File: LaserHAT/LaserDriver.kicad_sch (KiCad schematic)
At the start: 25 parts, among them J1 GPIO, J6 Conn_Coaxial, J7 Conn_Coaxial, U1 CAT24C32, U4 MCP1700x-330xxMB

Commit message: LaserHAT Rev 2: hand-routed HAT, laser + e-stim daughterboards, fab outputs
HAT (LaserHAT/):
- Rev 1 -> Rev 2 schematic migration (tools/rev2_migrate.py): issue #3 fixes,
  OLED bonnet kept, analog stage moved to plug-in daughterboards (J8/J9),
  buffered BNC I/O, USB-C power switch + PFET ideal diode.
- MCU pin map re-optimised for fewest vias: Pi UART on UART1 (PA8/PA9), I2C on
  PA0/PA1 (fail-safe), PWM_A/B on TIMA0 CCP1/CCP3 (PA7/PA12) with FAULT0 on PA6,
  active-low buttons.  Pi header: SWD swapped, NRST <-> MCU_POWER_EN swapped.
- Stable symbol UUIDs so KiCad "Update PCB" never replaces footprints.
- PCB placed and routed by hand; tidied (tools/track_tidy.py), silkscreen
  decluttered (tools/silk_declutter.py).  DRC clean apart from known cosmetic items.
- JLC fab outputs regenerated (fab/LaserHAT).
- CLAUDE.md, REV2_NOTES.md updated; portable Claude memory in claude_memory/.

Daughterboards: LaserDaughter (300 mA laser driver) and EStimDaughter (isolated
e-stim, imported from kbest/estim_module); interface spec in estim_interface/.

Firmware/Pi: `make flash HAT_REV=2` selects the Rev 2 header wiring;
Pi/power_cycle.py takes its power/reset pins from the environment.

Co-Authored-By: Claude Opus 5.5 <noreply@anthropic.com>
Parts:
- removed D10: D_Zener 6.2V, Diode_SMD:D_SOD-523, symbol Device:D_Zener
- removed D11: LED_ABGR, LED_SMD:LED_RGB_1210, symbol Device:LED_ABGR
- removed D6: 3v3, Diode_SMD:D_0603_1608Metric, symbol Device:LED
- removed D9: STIM, Diode_SMD:D_0603_1608Metric, symbol Device:LED
- removed J6, J7: Conn_Coaxial, Connector_Coaxial:BNC_Amphenol_031-5539_Vertical, symbol Connector:Conn_Coaxial
- removed R14: 200, Resistor_SMD:R_0402_1005Metric, symbol Device:R
- removed R16, R18: 470, Resistor_SMD:R_0402_1005Metric, symbol Device:R
- removed R17: 1k 1%, Resistor_SMD:R_0402_1005Metric, symbol Device:R
- added JP5: STANDALONE_3V3, Jumper:SolderJumper-2_P1.3mm_Open_RoundedPad1.0x1.5mm, symbol Jumper:SolderJumper_2_Open
- added R19, R20: 4.7k, Resistor_SMD:R_0402_1005Metric, symbol Device:R
- D7: value MSPM0 -> MCU
- JP4: value ID_WP -> RTS_NRST
- R13: value 1k 1% -> 3k
- R15: value 200 -> 2k
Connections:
- net +3V3: now also JP5.1 (A)
- net MCU_UART_RX: no longer J1.10 (Pin_10)
- net MCU_UART_TX: no longer J1.8 (Pin_8)
- net RPi +3V3: now also JP5.2 (B), R19.1, R20.1
- net EINK_BUSY renamed GPIO17
- net EINK_CIPO renamed GPIO9/SPI0.MISO
- net EINK_COPI renamed GPIO10/SPI0.MOSI
- net EINK_CS renamed GPIO8/SPI0.CE0
- net EINK_DC renamed GPIO22
- net EINK_RESET renamed GPIO27
- net EINK_SCK renamed GPIO11/SPI0.SCLK
- net GPIO26 renamed PI_TRIGGER
- net GPIO2/SDA1 renamed I2C_SDA
- net I2C_SDA: now also R19.2
- net GPIO3/SCL1 renamed I2C_SCL
- net I2C_SCL: now also R20.2
- net MCU_POWER_EN renamed GPIO18/PCM.CLK
- net GPIO18/PCM.CLK: now also J1.12 (Pin_12); no longer J1.16 (Pin_16)
- net MSPM0_3V3 renamed LED_MCU
- net MSPM0_NRST renamed GPIO23
- net GPIO23: now also J1.16 (Pin_16); no longer J1.12 (Pin_12)
- net MSPM0_SWCLK renamed GPIO25
- net MSPM0_SWDIO renamed GPIO24
- new net PI_RXD: J1.10 (Pin_10)
- new net PI_TXD: J1.8 (Pin_8)
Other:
- removed sheet EInk Display
- removed sheet Laser Driver Circuit
- added sheet BNC + Daughterboard I/O (bnc_daughter_io.kicad_sch)
- sheet MSPM0 Controller ports: added none; removed MSPM0_ADC, MSPM0_DAC, PWM_DUMMY, PWM_LASER, STIM_MIRROR, STIM_TRIGGER
- sheet USB-C UART ports: added none; removed 3v3_REG
- note added: "STAND-ALONE MODE (no Pi): close JP5 to power the OLED bonnet from the HAT 3.3 V regulator via header pins 1/17. OPEN JP5 BEFORE PLUGGING INTO A PI. R19/R20: I2C pull-ups for stand-alone use (parallel the Pi's 1k8 otherwise)."
- note removed: "TODO - Add in Rev 2. For now, can use an Adafruit Bonnet"

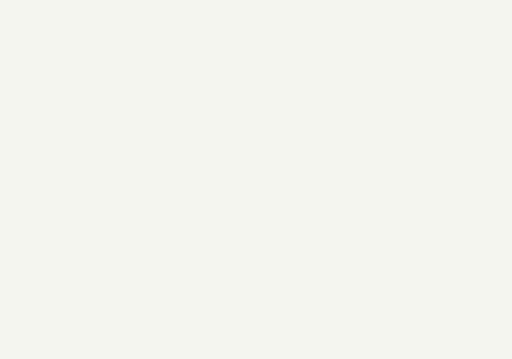
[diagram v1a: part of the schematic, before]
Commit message: LaserHAT: new owl logo (OwlLogo_Laser_14mm) with a paired schematic symbol so it survives F8
- Footprints.pretty/OwlLogo_Laser_14mm: the new owl-with-laser-eyes artwork (parts/kicad/OwlLogo)
  scaled by 0.891 to the old logo's 13.9 mm height; silk lines clamped at 0.15 mm, filled
  polygons keep zero-width strokes, copper beams 0.27 mm.
- LaserHAT.kicad_sym: OwlLogo graphic symbol (no pins, not in BOM), footprint pre-assigned.
  Library format bumped to 20231120.
- LaserDriver.kicad_sch: symbol G1 on the root sheet; LaserDriver.kicad_pcb: the old REF**
  RICE_OWL_LOGO replaced by G1 at (155.8, 66.8), linked by path, excluded from BOM/CPL.
- DRC: no electrical items, schematic parity clean; the logo's own silk-over-copper and
  mask-bridge warnings are by design (plot with "subtract soldermask from silkscreen").

Co-Authored-By: Claude Fable 5.1 <noreply@anthropic.com>
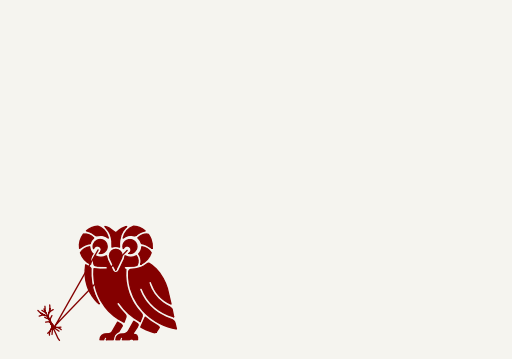
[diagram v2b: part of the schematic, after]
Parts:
- added G1: OwlLogo, Footprints:OwlLogo_Laser_14mm, symbol LaserHAT:OwlLogo
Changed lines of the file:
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@@
     )
   )
+	(symbol
+		(lib_id "LaserHAT:OwlLogo")
+		(at 25.4 275.0 0)
+		(unit 1)
+		(exclude_from_sim yes)
+		(in_bom no)
+		(on_board yes)
+		(dnp no)
+		(property "Reference" "G1"
+			(at 25.4 267.15 0)
+			(effects (font (size 1.27 1.27)) (hide yes))
+		)
+		(property "Value" "OwlLogo"
+			(at 25.4 282.85 0)
+			(effects (font (size 1.27 1.27)) (hide yes))
+		)
+		(property "Footprint" "Footprints:OwlLogo_Laser_14mm"
+			(at 25.4 275.0 0)
+			(effects (font (size 1.27 1.27)) (hide yes))
+		)
+		(property "Datasheet" ""
+			(at 25.4 275.0 0)
+			(effects (font (size 1.27 1.27)) (hide yes))
+		)
+		(property "Description" "Owl logo with laser eyes (graphic only, no pins); keeps the board logo through F8"
+			(at 25.4 275.0 0)
+			(effects (font (size 1.27 1.27)) (hide yes))
+		)
+		(instances
+			(project "LaserDriver"
+				(path "/e63e39d7-6ac0-4ffd-8aa3-1841a4541b55"
+					(reference "G1")
+					(unit 1)
+				)
+			)
+		)
+	)
 	(sheet_instances
 		(path "/"
